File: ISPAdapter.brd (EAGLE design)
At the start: 76 x 38 mm, 10 parts, among them U1 74LVC4066PW

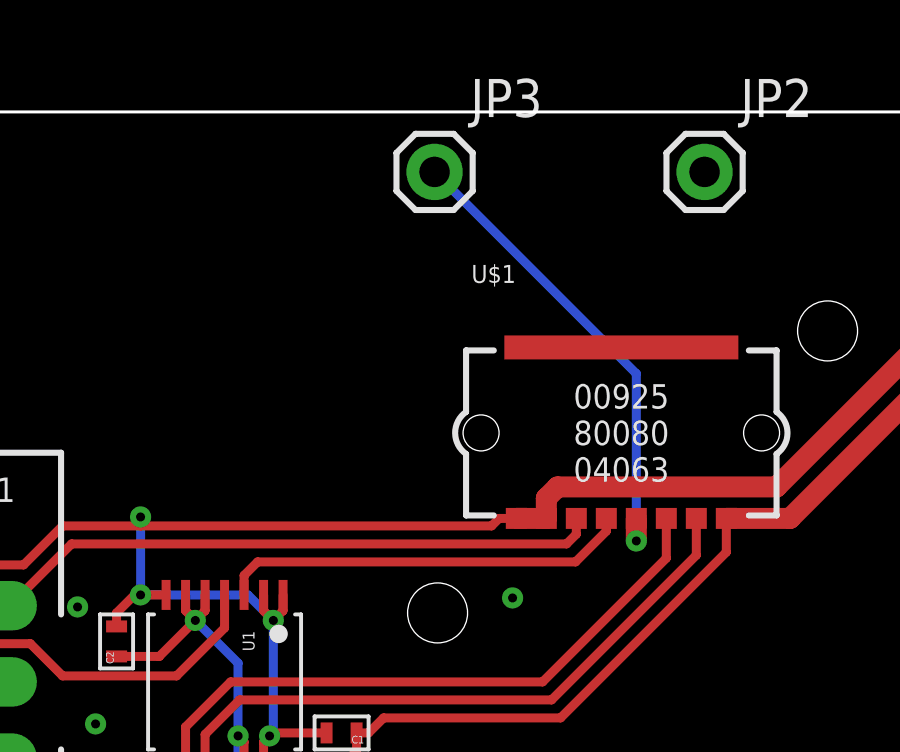
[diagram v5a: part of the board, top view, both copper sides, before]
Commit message: Layout updates, land pattern tweaks
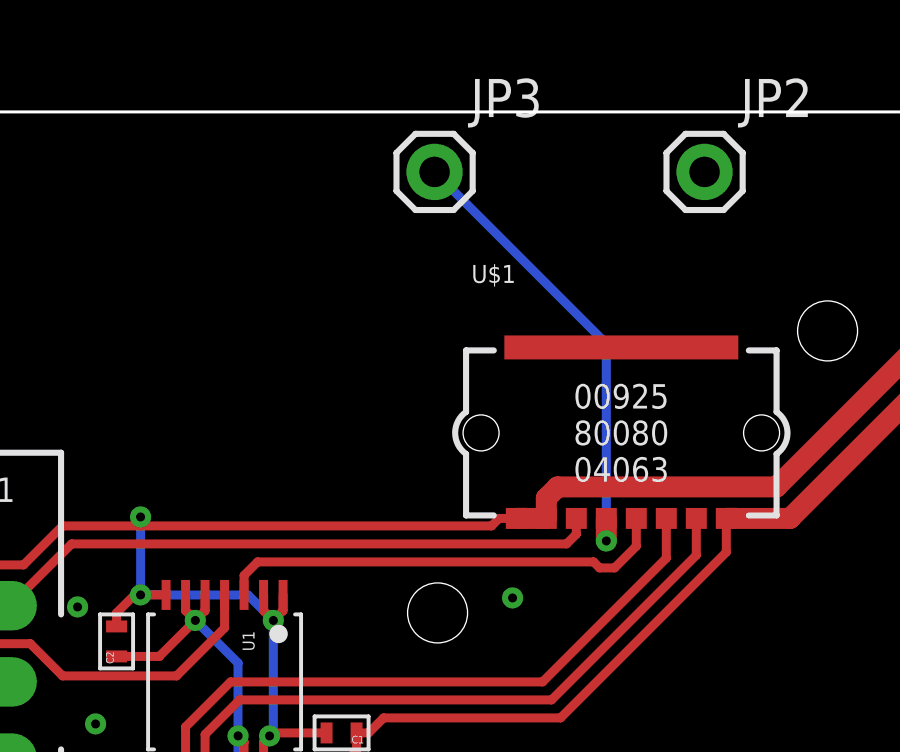
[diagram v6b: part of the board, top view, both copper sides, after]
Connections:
- net AUX: now also U$1.5; no longer U$1.4
- net MOSI: now also U$1.4; no longer U$1.5
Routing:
- net MOSI: track 13.8 -> 15.2 mm
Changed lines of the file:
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@@
 <grid distance="0.1" unitdist="mm" unit="mm" style="lines" multiple="10" display="yes" altdistance="0.025" altunitdist="mm" altunit="mm"/>
 <layers>
-<layer number="1" name="Top" color="4" fill="1" visible="yes" active="yes"/>
+<layer number="1" name="Top" color="4" fill="1" visible="no" active="yes"/>
 <layer number="2" name="Route2" color="1" fill="3" visible="no" active="no"/>
 <layer number="3" name="Route3" color="4" fill="3" visible="no" active="no"/>
 <layer number="14" name="Route14" color="1" fill="6" visible="no" active="no"/>
 <layer number="15" name="Route15" color="4" fill="6" visible="no" active="no"/>
-<layer number="16" name="Bottom" color="1" fill="1" visible="no" active="yes"/>
+<layer number="16" name="Bottom" color="1" fill="1" visible="yes" active="yes"/>
 <layer number="17" name="Pads" color="2" fill="1" visible="yes" active="yes"/>
 <layer number="18" name="Vias" color="2" fill="1" visible="yes" active="yes"/>
 <layer number="19" name="Unrouted" color="6" fill="1" visible="yes" active="yes"/>
 <layer number="20" name="Dimension" color="15" fill="1" visible="yes" active="yes"/>
-<layer number="21" name="tPlace" color="7" fill="1" visible="yes" active="yes"/>
-<layer number="22" name="bPlace" color="7" fill="1" visible="no" active="yes"/>
-<layer number="23" name="tOrigins" color="15" fill="1" visible="yes" active="yes"/>
-<layer number="24" name="bOrigins" color="15" fill="1" visible="no" active="yes"/>
+<layer number="21" name="tPlace" color="7" fill="1" visible="no" active="yes"/>
+<layer number="22" name="bPlace" color="7" fill="1" visible="yes" active="yes"/>
+<layer number="23" name="tOrigins" color="15" fill="1" visible="no" active="yes"/>
+<layer number="24" name="bOrigins" color="15" fill="1" visible="yes" active="yes"/>
 <layer number="25" name="tNames" color="7" fill="1" visible="no" active="yes"/>
 <layer number="26" name="bNames" color="7" fill="1" visible="no" active="yes"/>
 <layer number="27" name="tValues" color="7" fill="1" visible="no" active="yes"/>
 <layer number="28" name="bValues" color="7" fill="1" visible="no" active="yes"/>
-<layer number="29" name="tStop" color="7" fill="3" visible="yes" active="yes"/>
-<layer number="30" name="bStop" color="7" fill="6" visible="no" active="yes"/>
+<layer number="29" name="tStop" color="7" fill="3" visible="no" active="yes"/>
+<layer number="30" name="bStop" color="7" fill="6" visible="yes" active="yes"/>
 <layer number="31" name="tCream" color="7" fill="4" visible="no" active="yes"/>
-<layer number="32" name="bCream" color="7" fill="5" visible="no" active="yes"/>
-<layer number="33" name="tFinish" color="6" fill="3" visible="yes" active="yes"/>
-<layer number="34" name="bFinish" color="6" fill="6" visible="no" active="yes"/>
-<layer number="35" name="tGlue" color="7" fill="4" visible="yes" active="yes"/>
-<layer number="36" name="bGlue" color="7" fill="5" visible="no" active="yes"/>
-<layer number="37" name="tTest" color="7" fill="1" visible="yes" active="yes"/>
-<layer number="38" name="bTest" color="7" fill="1" visible="no" active="yes"/>
-<layer number="39" name="tKeepout" color="4" fill="11" visible="yes" active="yes"/>
-<layer number="40" name="bKeepout" color="1" fill="11" visible="no" active="yes"/>
-<layer number="41" name="tRestrict" color="4" fill="10" visible="yes" active="yes"/>
-<layer number="42" name="bRestrict" color="1" fill="10" visible="no" active="yes"/>
+<layer number="32" name="bCream" color="7" fill="5" visible="yes" active="yes"/>
+<layer number="33" name="tFinish" color="6" fill="3" visible="no" active="yes"/>
+<layer number="34" name="bFinish" color="6" fill="6" visible="yes" active="yes"/>
+<layer number="35" name="tGlue" color="7" fill="4" visible="no" active="yes"/>
+<layer number="36" name="bGlue" color="7" fill="5" visible="yes" active="yes"/>
+<layer number="37" name="tTest" color="7" fill="1" visible="no" active="yes"/>
+<layer number="38" name="bTest" color="7" fill="1" visible="yes" active="yes"/>
+<layer number="39" name="tKeepout" color="4" fill="11" visible="no" active="yes"/>
+<layer number="40" name="bKeepout" color="1" fill="11" visible="yes" active="yes"/>
+<layer number="41" name="tRestrict" color="4" fill="10" visible="no" active="yes"/>
+<layer number="42" name="bRestrict" color="1" fill="10" visible="yes" active="yes"/>
 <layer number="43" name="vRestrict" color="2" fill="10" visible="no" active="yes"/>
 <layer number="44" name="Drills" color="7" fill="1" visible="no" active="yes"/>
@@
 <layer number="46" name="Milling" color="3" fill="1" visible="no" active="yes"/>
 <layer number="47" name="Measures" color="7" fill="1" visible="yes" active="yes"/>
-<layer number="48" name="Document" color="7" fill="1" visible="no" active="yes"/>
+<layer number="48" name="Document" color="7" fill="1" visible="yes" active="yes"/>
 <layer number="49" name="Reference" color="7" fill="1" visible="no" active="yes"/>
 <layer number="50" name="dxf" color="7" fill="1" visible="no" active="no"/>
-<layer number="51" name="tDocu" color="7" fill="1" visible="yes" active="yes"/>
-<layer number="52" name="bDocu" color="7" fill="1" visible="no" active="yes"/>
+<layer number="51" name="tDocu" color="7" fill="1" visible="no" active="yes"/>
+<layer number="52" name="bDocu" color="7" fill="1" visible="yes" active="yes"/>
 <layer number="53" name="tGND_GNDA" color="7" fill="9" visible="no" active="no"/>
 <layer number="54" name="bGND_GNDA" color="1" fill="9" visible="no" active="no"/>
@@
 <layer number="100" name="Muster" color="7" fill="1" visible="no" active="no"/>
 <layer number="101" name="Patch_Top" color="12" fill="4" visible="no" active="yes"/>
-<layer number="102" name="Vscore" color="7" fill="1" visible="yes" active="yes"/>
+<layer number="102" name="Vscore" color="7" fill="1" visible="no" active="yes"/>
 <layer number="103" name="tMap" color="7" fill="1" visible="no" active="yes"/>
 <layer number="104" name="Name" color="16" fill="1" visible="no" active="yes"/>
-<layer number="105" name="tPlate" color="7" fill="1" visible="yes" active="yes"/>
+<layer number="105" name="tPlate" color="7" fill="1" visible="no" active="yes"/>
 <layer number="106" name="bPlate" color="7" fill="1" visible="no" active="yes"/>
-<layer number="107" name="tLabels" color="7" fill="1" visible="yes" active="yes"/>
+<layer number="107" name="tLabels" color="7" fill="1" visible="no" active="yes"/>
 <layer number="108" name="tplace-old" color="10" fill="1" visible="no" active="yes"/>
 <layer number="109" name="ref-old" color="11" fill="1" visible="no" active="yes"/>
@@
 <text x="32.8" y="23.7" size="0.8128" layer="107" font="vector" ratio="15" align="top-center">2</text>
 <text x="31.8" y="23.7" size="0.8128" layer="107" font="vector" ratio="15" align="top-center">3</text>
-<text x="28.8" y="23.7" size="0.8128" layer="107" font="vector" ratio="15" align="top-center">4</text>
+<text x="29.8" y="23.7" size="0.8128" layer="107" font="vector" ratio="15" align="top-center">4</text>
 <text x="27.8" y="23.7" size="0.8128" layer="107" font="vector" ratio="15" align="top-center">5</text>
 <text x="26.8" y="23.7" size="0.8128" layer="107" font="vector" ratio="15" align="top-center">6</text>
@@
 </signal>
 <signal name="MOSI">
-<contactref element="U$1" pad="5"/>
-<wire x1="28.725" y1="24.45" x2="28.725" y2="24.025" width="0.3" layer="1"/>
-<wire x1="28.725" y1="24.025" x2="27.7" y2="23" width="0.3" layer="1"/>
-<wire x1="27.7" y1="23" x2="17.1" y2="23" width="0.3" layer="1"/>
+<wire x1="28.3" y1="23" x2="17.1" y2="23" width="0.3" layer="1"/>
 <wire x1="16.65" y1="22.55" x2="17.1" y2="23" width="0.3" layer="1"/>
 <contactref element="U1" pad="3"/>
 <wire x1="16.65" y1="22.55" x2="16.65" y2="21.9" width="0.3" layer="1"/>
+<contactref element="U$1" pad="4"/>
+<wire x1="29.725" y1="24.45" x2="29.725" y2="23.525" width="0.3" layer="1"/>
+<wire x1="29.725" y1="23.525" x2="29" y2="22.8" width="0.3" layer="1"/>
+<wire x1="29" y1="22.8" x2="28.5" y2="22.8" width="0.3" layer="1"/>
+<wire x1="28.5" y1="22.8" x2="28.3" y2="23" width="0.3" layer="1"/>
 </signal>
 <signal name="DGND">
@@
 </signal>
 <signal name="AUX">
-<contactref element="U$1" pad="4"/>
 <contactref element="JP3" pad="1"/>
-<via x="29.725" y="23.7" extent="1-16" drill="0.3"/>
-<wire x1="29.725" y1="24.45" x2="29.725" y2="23.7" width="0.7" layer="1"/>
-<wire x1="29.725" y1="29.275" x2="23" y2="36" width="0.3" layer="16"/>
-<wire x1="29.725" y1="29.275" x2="29.725" y2="23.7" width="0.3" layer="16"/>
+<via x="28.725" y="23.7" extent="1-16" drill="0.3"/>
+<contactref element="U$1" pad="5"/>
+<wire x1="28.725" y1="24.45" x2="28.725" y2="23.7" width="0.7" layer="1"/>
+<wire x1="28.725" y1="23.7" x2="28.725" y2="30.275" width="0.3" layer="16"/>
+<wire x1="28.725" y1="30.275" x2="23" y2="36" width="0.3" layer="16"/>
 </signal>
 <signal name="ISP_EN">
